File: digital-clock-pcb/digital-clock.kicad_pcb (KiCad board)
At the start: 2 copper layers, 50 x 100 mm, 31 parts, among them J1 USB_OTG, J2 Conn_02x03_Odd_Even, J3 OUT, J4 IN, U1 ATmega328P-M, U2 PCF8523T, Y1 ABS2532768KHZ6T

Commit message: change m328 package
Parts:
- J3: value OUT -> Conn_01x04
- J4: value IN -> Conn_01x04
- U1: footprint Package_DFN_QFN:QFN-32-1EP_5x5mm_P0.5mm_EP3.1x3.1mm -> Package_QFP:TQFP-32_7x7mm_P0.8mm
- moved U1 4.05 mm to (129.3, 106.5)
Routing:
- net SCL: track 24.4 -> 28.3 mm
- net SDA: track 14.5 -> 18.2 mm
- net GND: track 6.90 -> 10.3 mm, vias 17 -> 18
- net VCC: track 324.8 -> 327.0 mm, vias 5 -> 6
- net MISO: track 6.61 -> 8.81 mm
- net Net-(D14-Pad4): track 17.0 -> 14.9 mm
- net RST: track 23.3 -> 25.3 mm
- net SCK: track 8.94 -> 10.6 mm
- net MOSI: track 6.17 -> 7.31 mm

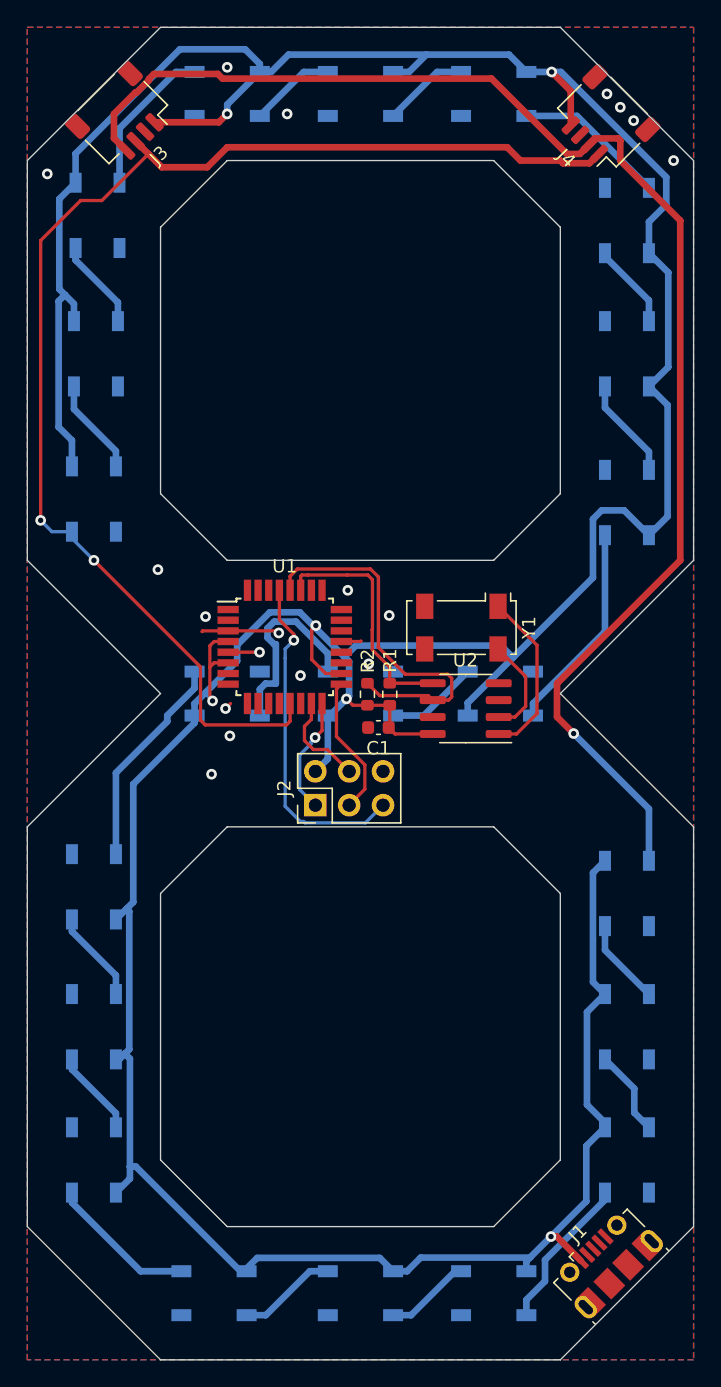
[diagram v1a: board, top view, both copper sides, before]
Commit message: add clock battery + add button for change hour and minute
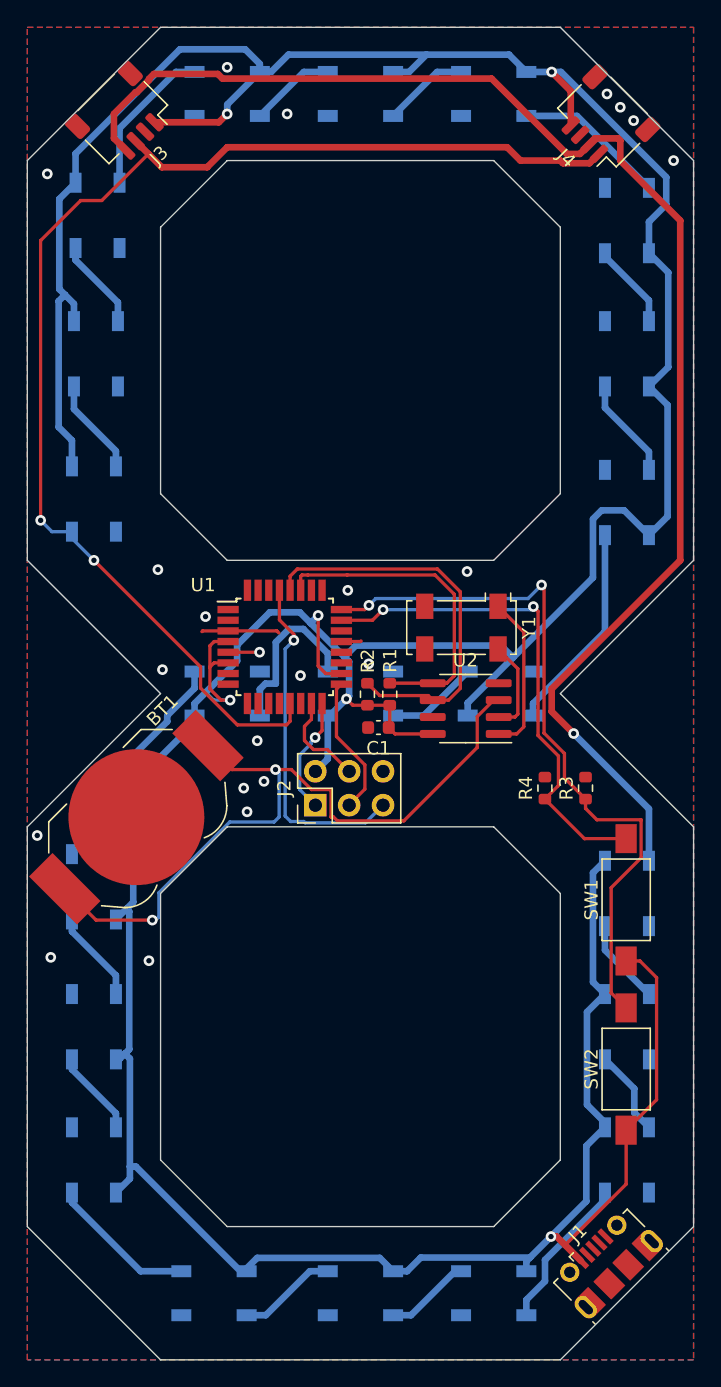
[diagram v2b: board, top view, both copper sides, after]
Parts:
- added BT1: Battery_Cell, Battery:BatteryHolder_LINX_BAT-HLD-012-SMT, F.Cu at (118.2, 119.3)
- added R3: R_Small, Resistor_SMD:R_0603_1608Metric, F.Cu at (151.9, 117.1)
- added R4: R_Small, Resistor_SMD:R_0603_1608Metric, F.Cu at (148.8, 117.1)
- added SW1: SW_SPST, Button_Switch_SMD:SW_SPST_FSMSM, F.Cu at (154.9, 125.5)
- added SW2: SW_SPST, Button_Switch_SMD:SW_SPST_FSMSM, F.Cu at (154.9, 138.2)
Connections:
- U1 pad 23: unconnected-(U1-Pad23) -> BTN1
- U1 pad 24: unconnected-(U1-Pad24) -> BTN2
- U2 pad 3: unconnected-(U2-Pad3) -> Net-(BT1-+)
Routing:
- net Net-(BT1-+): track 0.00 -> 55.5 mm, vias 0 -> 2
- net BTN2: track 0.00 -> 54.0 mm, vias 0 -> 2
- net BTN1: track 0.00 -> 37.8 mm, vias 0 -> 2
- net VCC: track 327.0 -> 356.1 mm
- net SDA: track 18.2 -> 24.4 mm
- net Net-(D14-DIN): track 14.9 -> 12.9 mm
- net SCL: track 28.3 -> 29.9 mm
- net WS_IN: track 97.9 -> 96.5 mm
- net Net-(U2-OSCI): track 12.8 -> 12.0 mm
- net GND: track 10.3 -> 9.72 mm, vias 18 -> 22

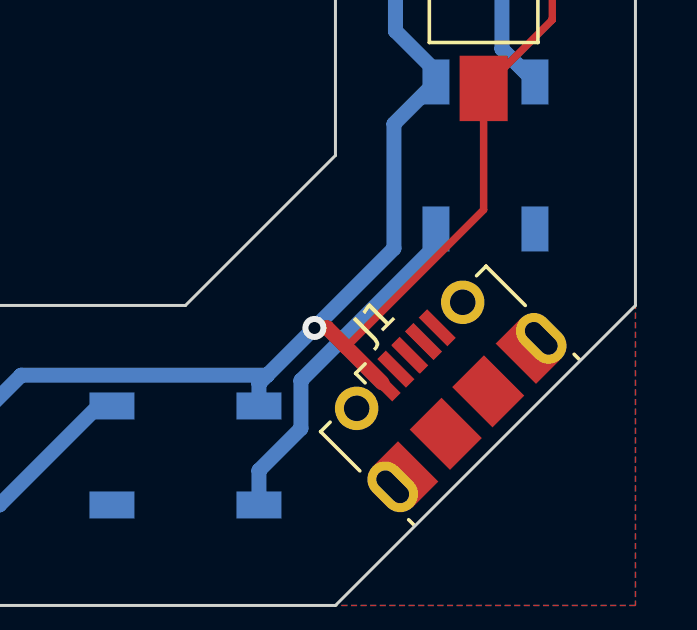
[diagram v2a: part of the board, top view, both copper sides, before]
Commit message: add gnd usb
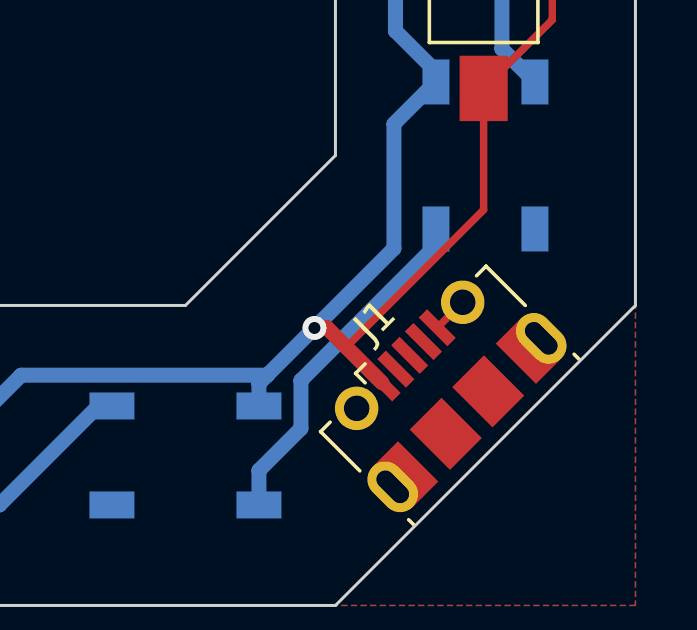
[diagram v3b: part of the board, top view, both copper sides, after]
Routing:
- net GND: track 9.72 -> 10.9 mm
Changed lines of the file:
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@@
   (segment (start 123.155731 105.294269) (end 123.1 105.35) (width 0.25) (layer "F.Cu") (net 23))
   (segment (start 125.069396 105.294269) (end 128.719269 105.294269) (width 0.25) (layer "F.Cu") (net 23))
+  (segment (start 153.394263 150.742426) (end 154.242791 149.893897) (width 0.25) (layer "F.Cu") (net 23))
   (segment (start 128.719269 105.294269) (end 128.875 105.45) (width 0.25) (layer "F.Cu") (net 23))
   (via (at 111.76 129.794) (size 0.8) (drill 0.4) (layers "F.Cu" "B.Cu") (free) (net 23))
